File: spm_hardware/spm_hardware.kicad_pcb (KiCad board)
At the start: 2 copper layers, 57 parts, among them J1 Magnet sensor, J2 Floater, J3 MotIn, J4 MotOut, J5 230VAC, J6 USonic sensor, J7 Temp&Humid sensor, J8 Flow sensor, J9 HAL sensor, P1 DIL16, Q1 BS170, T1 Transformer_1P_1S, U1 G3MB-202P, U2 ESP-12E, U3 STM32L432, U4 LTV-817, U5 LTV-817

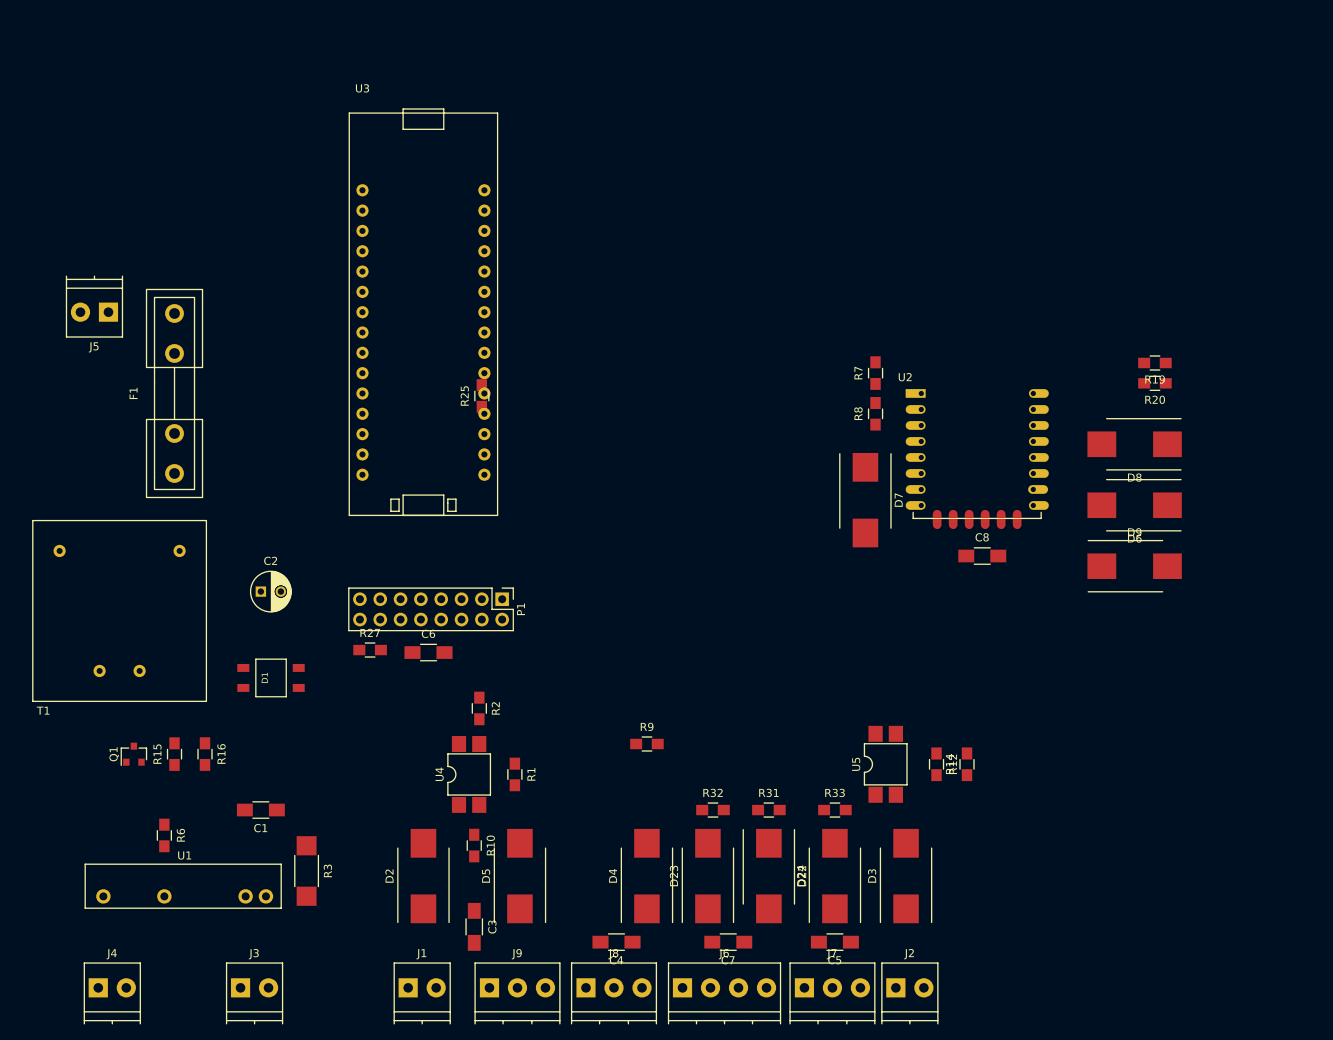
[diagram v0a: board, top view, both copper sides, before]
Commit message: Change fuse for smaller one
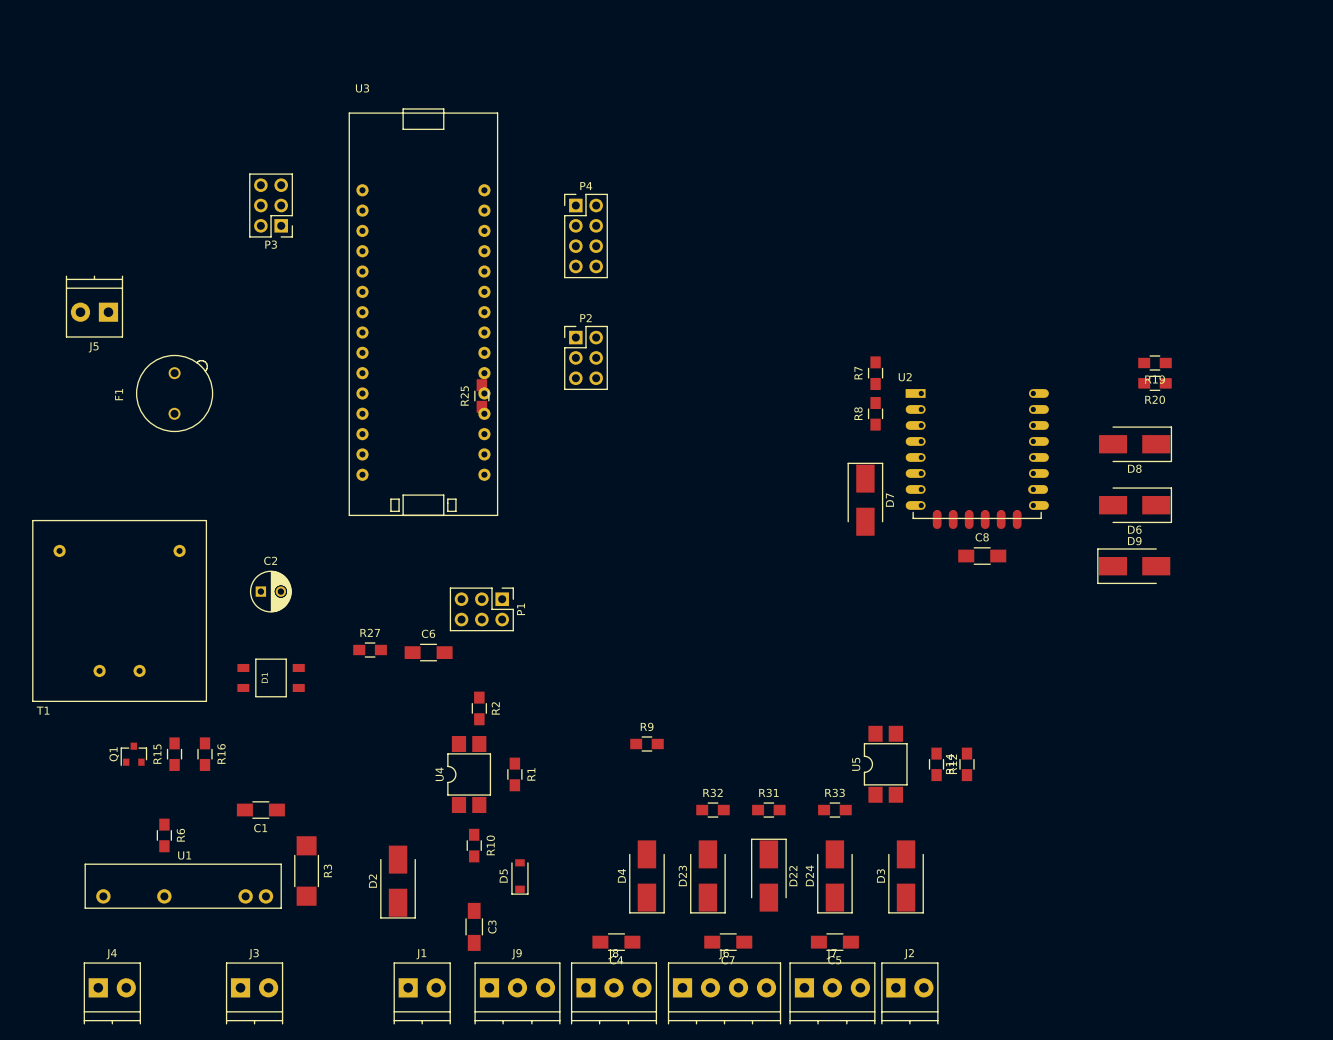
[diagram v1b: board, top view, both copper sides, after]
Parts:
- added P2: DIL6, Pin_Headers:Pin_Header_Straight_2x03_Pitch2.54mm, F.Cu at (93.3, 88.3)
- added P3: DIL6, Pin_Headers:Pin_Header_Straight_2x03_Pitch2.54mm, F.Cu at (56.5, 74.3)
- added P4: DIL8, Pin_Headers:Pin_Header_Straight_2x04_Pitch2.54mm, F.Cu at (93.3, 71.8)
- D2, D22, D23, D24, D3, D4, D6, D7, D8, D9: footprint Diodes_SMD:DO-214AB_Handsoldering -> Diodes_SMD:D_SMB_Handsoldering
- D5: footprint Diodes_SMD:DO-214AB_Handsoldering -> Diodes_SMD:D_SOD-123
- F1: footprint Fuse_Holders_and_Fuses:Fuseholder5x20_horiz_open_inline_Type-I -> Fuse_Holders_and_Fuses:Fuseholder_Fuse_TR5_Littlefuse-No560_No460
- P1: value DIL16 -> DIL6; footprint Pin_Headers:Pin_Header_Straight_2x08_Pitch2.54mm -> Pin_Headers:Pin_Header_Straight_2x03_Pitch2.54mm
- moved D2 3.24 mm to (71.1, 156.2)
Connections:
- J7 pad 2: Net-(J7-Pad2) -> Net-(D24-Pad1)
- P1 pad 2: SPI_CS -> SPI_MISO
- P1 pad 4: SPI_MISO -> SPI_CLK
- P1 pad 5: SPI_CLK -> SPI_CS
- P1 pad 6: PA8/TIM_CH1 -> +3V3
- R25 pad 1: +3V3 -> I2C_CLK
- R25 pad 2: I2C_CLK -> +3V3
- R27 pad 1: +3V3 -> I2C_SDA
- R27 pad 2: I2C_SDA -> +3V3
- U2 pad 10: Net-(U2-Pad10) -> (no net)
- U2 pad 11: Net-(U2-Pad11) -> (no net)
- U2 pad 12: Net-(U2-Pad12) -> (no net)
- U2 pad 13: Net-(U2-Pad13) -> (no net)
- U2 pad 14: Net-(U2-Pad14) -> (no net)
- U2 pad 17: Net-(U2-Pad17) -> (no net)
- U2 pad 18: Net-(U2-Pad18) -> (no net)
- U2 pad 19: Net-(U2-Pad19) -> (no net)
- U2 pad 2: Net-(U2-Pad2) -> (no net)
- U2 pad 20: Net-(U2-Pad20) -> (no net)
- U2 pad 21: Net-(U2-Pad21) -> (no net)
- U2 pad 22: Net-(U2-Pad22) -> (no net)
- U2 pad 4: Net-(U2-Pad4) -> (no net)
- U2 pad 5: Net-(U2-Pad5) -> (no net)
- U2 pad 6: Net-(U2-Pad6) -> (no net)
- U2 pad 7: Net-(U2-Pad7) -> (no net)
- U3 pad 18: Net-(U3-Pad18) -> (no net)
- U3 pad 28: Net-(U3-Pad28) -> (no net)
- U3 pad 3: Net-(U3-Pad3) -> (no net)

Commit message: Layout the PCB
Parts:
- moved R20 76.7 mm to (104.1, 139.7), turned to 270 degrees
- moved R19 71.9 mm to (113.0, 140.3), turned to 90 degrees
- moved D9 67.5 mm to (99.7, 139.7), turned to 270 degrees
- moved D8 66.6 mm to (108.6, 139.7), turned to 90 degrees
- moved P4 64.2 mm to (90.8, 135.9)
- moved C8 45.5 mm to (99.7, 106.0), turned to 90 degrees
- moved D6 44.6 mm to (118.7, 105.4), turned to 270 degrees
- moved P3 43.6 mm to (62.9, 117.5)
- moved U3 41.3 mm to (67.9, 146.7)
- moved C6 39.1 mm to (101.6, 156.2), turned to 90 degrees
- moved J3 37.5 mm to (27.9, 140.3), turned to 270 degrees
- moved R25 25.8 mm to (97.2, 116.2), turned to 270 degrees
- moved U2 25.6 mm to (118.7, 113.7), turned to 270 degrees
- moved P2 25.5 mm to (90.8, 113.7)
- moved R32 25.5 mm to (86.4, 155.6), turned to 90 degrees
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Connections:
- U1 pad 1: Net-(J3-Pad1) -> Net-(C1-Pad2)
- U1 pad 2: Net-(C1-Pad2) -> Net-(J3-Pad1)
- U1 pad 3: Net-(R6-Pad2) -> Net-(Q1-Pad1)
- U1 pad 4: Net-(Q1-Pad1) -> Net-(R6-Pad2)
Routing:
- net GND: track 0.00 -> 426.7 mm, vias 0 -> 4
- net +5V: track 0.00 -> 199.2 mm
- net +3V3: track 0.00 -> 151.3 mm
- net USART1_RX: track 0.00 -> 72.4 mm, vias 0 -> 1
- net Floater: track 0.00 -> 66.9 mm
- net WIFI_RST: track 0.00 -> 57.1 mm
- net USART1_TX: track 0.00 -> 55.7 mm, vias 0 -> 1
- net WIFI_EN: track 0.00 -> 54.0 mm
- net +12V: track 0.00 -> 42.0 mm
- net TH_Sensor: track 0.00 -> 39.5 mm
- net SPI_CLK: track 0.00 -> 36.6 mm
- net HAL_Sen: track 0.00 -> 36.6 mm, vias 0 -> 2
- net Flow_Sen: track 0.00 -> 35.2 mm, vias 0 -> 1
- net USonic_trigger: track 0.00 -> 33.7 mm, vias 0 -> 1
- net PB0/TIM_CH2N: track 0.00 -> 28.9 mm, vias 0 -> 1
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- added copper zone on B.Cu, net GND
- added copper zone on F.Cu, net GND
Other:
- net class 12V added: clearance 0.2, trace_width 0.5, via_dia 0.6, via_drill 0.4
- net class 230V added: clearance 0.5, trace_width 0.75, via_dia 1.2, via_drill 0.5
- net class 5V added: clearance 0.2, trace_width 0.35, via_dia 0.6, via_drill 0.4

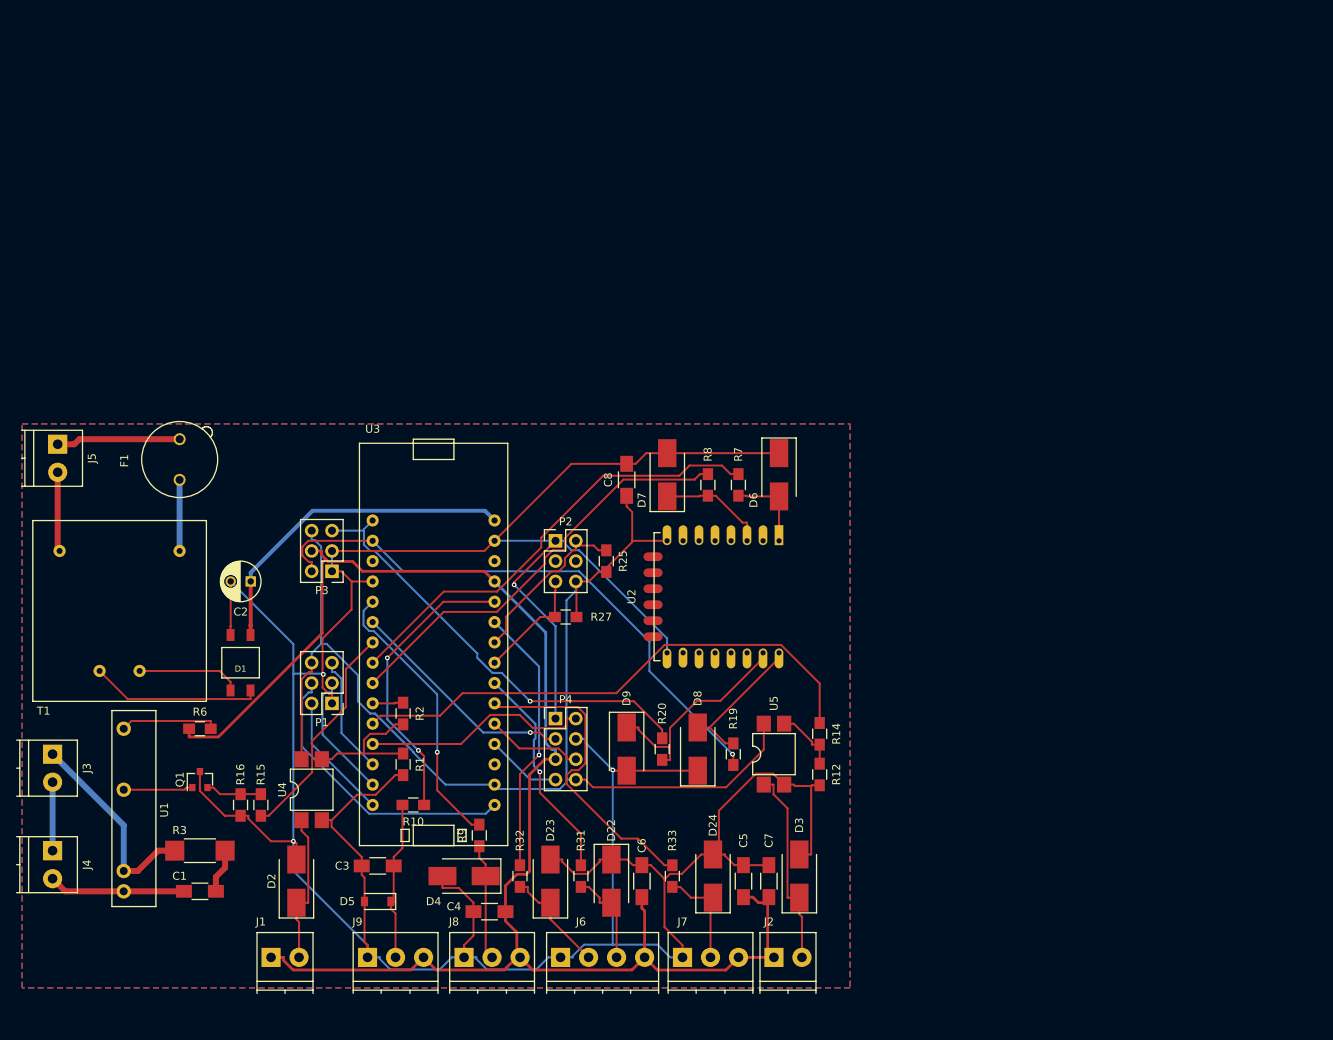
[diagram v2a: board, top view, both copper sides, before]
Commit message: Adapt the PCB layout for a box
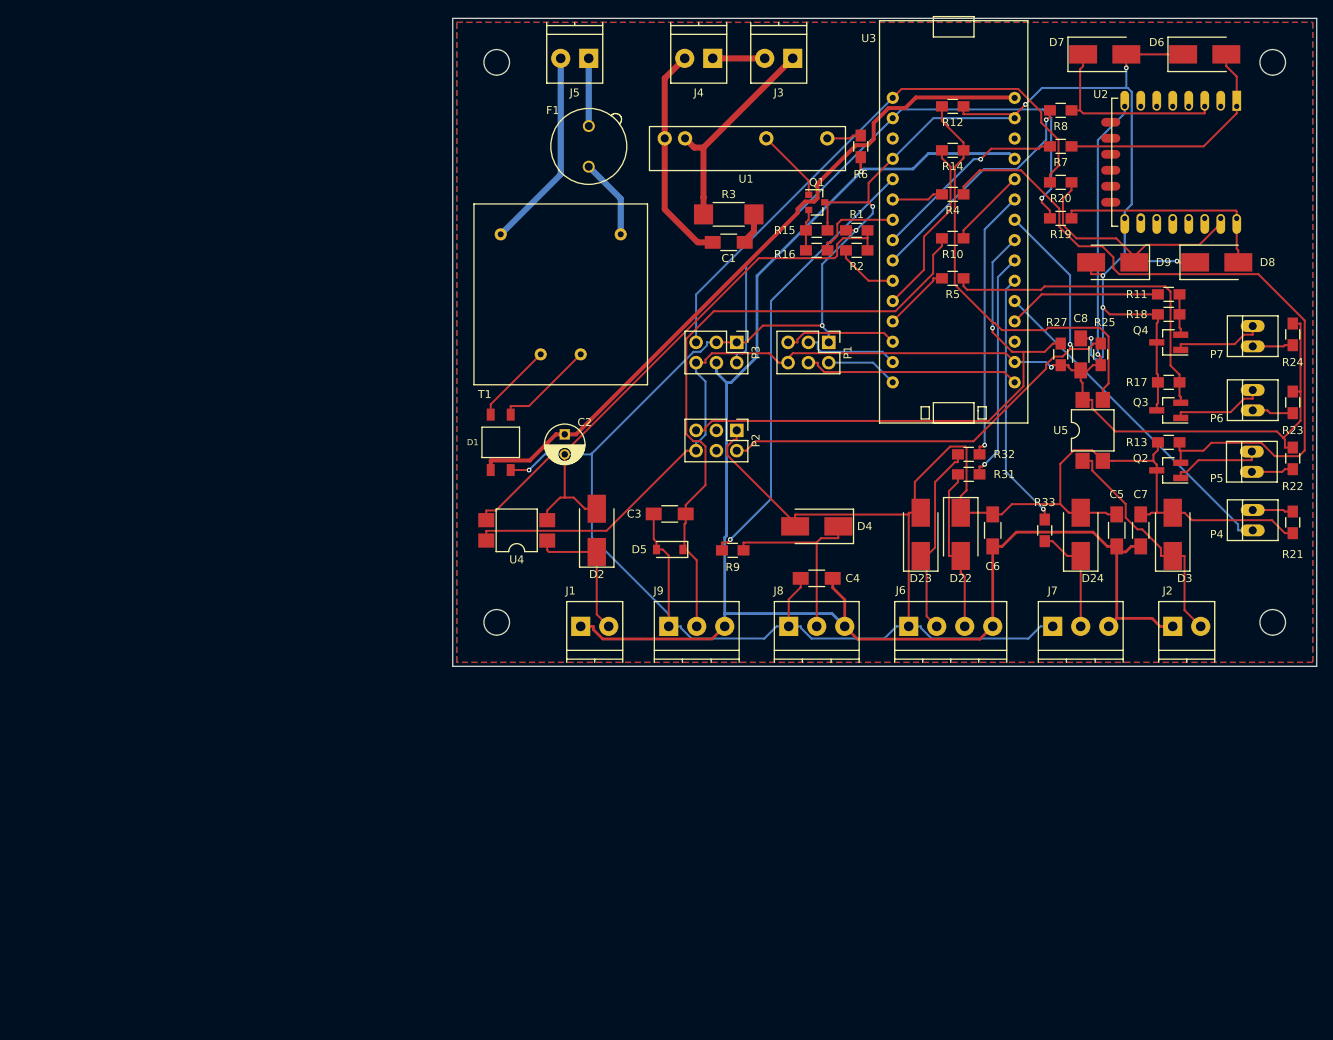
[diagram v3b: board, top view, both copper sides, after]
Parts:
- added P5: CONN_01X02, Connectors:PINHEAD1-2, F.Cu at (177.8, 105.0)
- added P6: CONN_01X02, Connectors:PINHEAD1-2, F.Cu at (178.0, 97.4)
- added P7: CONN_01X02, Connectors:PINHEAD1-2, F.Cu at (178.0, 89.4)
- added Q2: Q_NMOS_DGS, TO_SOT_Packages_SMD:SOT-23_Handsoldering, F.Cu at (167.5, 104.9)
- added Q3: Q_NMOS_DGS, TO_SOT_Packages_SMD:SOT-23_Handsoldering, F.Cu at (167.5, 97.4)
- added Q4: Q_NMOS_DGS, TO_SOT_Packages_SMD:SOT-23_Handsoldering, F.Cu at (167.5, 88.9)
- added R11: R, Resistors_SMD:R_0805_HandSoldering, F.Cu at (167.5, 82.9)
- added R13: R, Resistors_SMD:R_0805_HandSoldering, F.Cu at (167.5, 101.4)
- added R17: R, Resistors_SMD:R_0805_HandSoldering, F.Cu at (167.5, 93.9)
- added R18: R, Resistors_SMD:R_0805_HandSoldering, F.Cu at (167.5, 85.4)
- added R21: R, Resistors_SMD:R_0805_HandSoldering, F.Cu at (183.0, 111.4)
- added R22: R, Resistors_SMD:R_0805_HandSoldering, F.Cu at (183.0, 103.4)
- added R23: R, Resistors_SMD:R_0805_HandSoldering, F.Cu at (183.0, 96.4)
- added R24: R, Resistors_SMD:R_0805_HandSoldering, F.Cu at (183.0, 87.9)
- added R4: R, Resistors_SMD:R_0805_HandSoldering, F.Cu at (140.5, 70.4)
- added R5: R, Resistors_SMD:R_0805_HandSoldering, F.Cu at (140.5, 80.9)
- P4: value DIL8 -> CONN_01X02; footprint Pin_Headers:Pin_Header_Straight_2x04_Pitch2.54mm -> Connectors:PINHEAD1-2
- moved J4 128.9 mm to (110.5, 53.4), turned to 180 degrees
- moved J3 127.0 mm to (120.5, 53.4), turned to 180 degrees
- moved U1 115.9 mm to (104.5, 63.4), turned to 0 degrees
- moved R6 110.1 mm to (129.0, 64.4), turned to 90 degrees
- moved Q1 105.6 mm to (123.5, 71.4), turned to 0 degrees
- moved C1 104.6 mm to (112.5, 76.4)
- moved R3 103.4 mm to (112.5, 72.9)
- moved R15 101.7 mm to (123.5, 74.9), turned to 0 degrees
- moved R16 98.2 mm to (123.5, 77.4), turned to 180 degrees
- moved R10 97.8 mm to (140.5, 75.9)
- moved P4 90.3 mm to (178.0, 112.4), turned to 90 degrees
- moved D8 88.9 mm to (173.5, 78.9), turned to 0 degrees
- moved R1 87.6 mm to (128.5, 74.9), turned to 180 degrees
- moved R20 86.6 mm to (154.0, 68.9), turned to 0 degrees
- moved D9 86.0 mm to (160.5, 78.9), turned to 180 degrees
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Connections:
- P4 pad 1: GND -> Btn_ctrl
- P4 pad 2: PA8/TIM_CH1 -> Net-(P4-Pad2)
- U3 pad 12: PA8/TIM_CH1 -> LED_WiFi
- U3 pad 26: PA1/ADC12_IN6 -> Btn_ctrl
- U3 pad 27: PA0/ADC12_IN5 -> LED_Status
- U3 pad 6: PB0/TIM_CH2N -> LED_Trip
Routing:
- net Net-(Q2-Pad2): track 0.00 -> 90.2 mm
- net Net-(C3-Pad1): track 20.4 -> 78.5 mm
- net I2C_SDA: track 14.4 -> 70.3 mm, vias 0 -> 1
- net I2C_CLK: track 21.7 -> 70.4 mm, vias 0 -> 1
- net Net-(R1-Pad1): track 17.9 -> 66.3 mm
- net +12V: track 42.0 -> 88.1 mm
- net Net-(R12-Pad1): track 8.33 -> 54.2 mm
- net Floater: track 66.9 -> 22.3 mm
- net Btn_ctrl: track 0.00 -> 42.1 mm
- net Net-(Q3-Pad2): track 0.00 -> 41.9 mm
- net WIFI_RST: track 57.1 -> 24.5 mm, vias 0 -> 1
- net +3V3: track 151.3 -> 183.1 mm, vias 0 -> 2
- net GND: track 426.7 -> 457.8 mm, vias 4 -> 10
- net PB0/TIM_CH2N: track 28.9 -> 0.00 mm, vias 1 -> 0
- net PA8/TIM_CH1: track 28.5 -> 0.00 mm
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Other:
- board outline added: 108 x 81 mm
